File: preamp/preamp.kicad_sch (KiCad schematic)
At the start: 20 parts, among them J1 XLR3_AudioJack2_Combo, J2 Output, J3 Conn_Coaxial, J4 AudioJack3_Switch, U1 SSM2019

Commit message: Prepare for routing
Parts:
- removed unit 2 of J1
- C7: renamed from C?; footprint Capacitor_THT:C_Disc_D3.0mm_W1.6mm_P2.50mm -> Capacitor_THT:C_Rect_L7.0mm_W2.5mm_P5.00mm
- J1: footprint Connector_Audio:Jack_XLR-6.35mm_Neutrik_NCJ9FI-V-0_Vertical -> Connector_Audio:Jack_XLR_Neutrik_NC3FAAH2_Horizontal

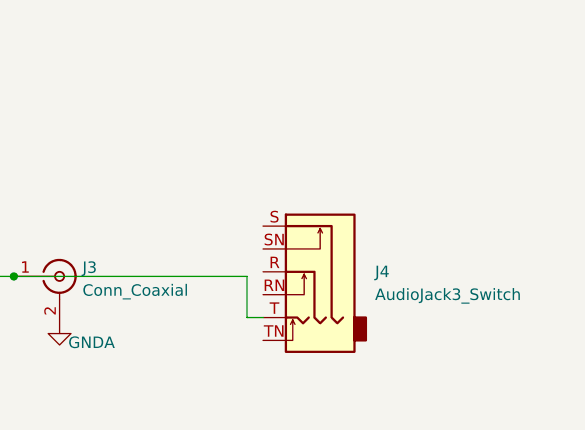
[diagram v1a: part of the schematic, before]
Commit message: Add RCA Plug
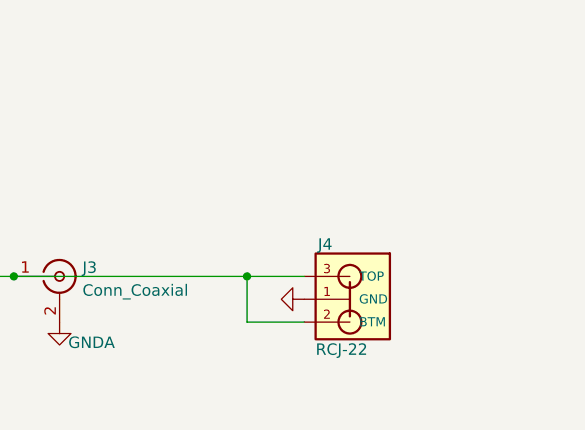
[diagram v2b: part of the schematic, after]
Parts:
- removed J4: AudioJack3_Switch, Connector_Audio:Jack_6.35mm_Neutrik_NMJ6HFD2-AU_Horizontal, symbol Connector:AudioJack3_Switch
- added J4: RCJ-22, rcj-22:rcj-22, symbol rcj-22:RCJ-22
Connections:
- net GNDA: now also J4.1 (GND)
- net at C7.2, J2.2 (Pin_2), J3.1 (In): now also J4.2 (BTM), J4.3 (TOP)
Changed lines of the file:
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@@
   (junction (at 69.85 62.738) (diameter 0) (color 0 0 0 0)
+  )
+  (junction (at 203.708 83.566) (diameter 0) (color 0 0 0 0)
   )
   (junction (at 98.298 82.55) (diameter 0) (color 0 0 0 0)
@@
     (stroke (width 0) (type default) (color 0 0 0 0))
   )
+  (wire (pts (xy 210.058 88.646) (xy 203.708 88.646))
+    (stroke (width 0) (type default) (color 0 0 0 0))
+  )
   (wire (pts (xy 100.076 74.93) (xy 90.678 74.93))
     (stroke (width 0) (type default) (color 0 0 0 0))
   )
-  (wire (pts (xy 203.708 88.138) (xy 205.486 88.138))
-    (stroke (width 0) (type default) (color 0 0 0 0))
-  )
   (wire (pts (xy 109.728 74.93) (xy 114.808 74.93))
     (stroke (width 0) (type default) (color 0 0 0 0))
@@
     (stroke (width 0) (type default) (color 0 0 0 0))
   )
-  (wire (pts (xy 203.708 83.566) (xy 203.708 88.138))
+  (wire (pts (xy 203.708 88.646) (xy 203.708 83.566))
+    (stroke (width 0) (type default) (color 0 0 0 0))
+  )
+  (wire (pts (xy 203.708 83.566) (xy 210.058 83.566))
     (stroke (width 0) (type default) (color 0 0 0 0))
   )
@@
     (pin "1")
     (pin "2")
+  )
+  (symbol (lib_id "rcj-22:RCJ-22") (at 213.868 86.106 0) (mirror y) (unit 1)
+    (in_bom yes) (on_board yes)
+    (property "Reference" "J4" (id 0) (at 211.582 80.01 0)
+      (effects (font (size 1.27 1.27)) (justify right))
+    )
+    (property "Value" "RCJ-22" (id 1) (at 211.328 91.694 0)
+      (effects (font (size 1.27 1.27)) (justify right))
+    )
+    (property "Footprint" "rcj-22:rcj-22" (id 2) (at 215.773 94.996 0)
+      (effects (font (size 1.27 1.27)) (justify bottom) hide)
+    )
+    (property "Datasheet" "" (id 3) (at 198.628 96.266 0)
+      (effects (font (size 1.27 1.27)) hide)
+    )
+    (pin "1")
+    (pin "2")
+    (pin "3")
   )
   (symbol (lib_id "power:GNDA") (at 69.85 62.738 90) (unit 1)
@@
     (pin "2")
   )
-  (symbol (lib_id "Connector:AudioJack3_Switch") (at 210.566 83.058 0) (mirror y) (unit 1)
-    (in_bom yes) (on_board yes) (fields_autoplaced)
-    (property "Reference" "J4" (id 0) (at 217.932 83.0579 0)
-      (effects (font (size 1.27 1.27)) (justify right))
-    )
-    (property "Value" "AudioJack3_Switch" (id 1) (at 217.932 85.5979 0)
-      (effects (font (size 1.27 1.27)) (justify right))
-    )
-    (property "Footprint" "Connector_Audio:Jack_6.35mm_Neutrik_NMJ6HFD2-AU_Horizontal" (id 2) (at 210.566 83.058 0)
-      (effects (font (size 1.27 1.27)) hide)
-    )
-    (property "Datasheet" "~" (id 3) (at 210.566 83.058 0)
-      (effects (font (size 1.27 1.27)) hide)
-    )
-    (pin "R")
-    (pin "RN")
-    (pin "S")
-    (pin "SN")
-    (pin "T")
-    (pin "TN")
+  (symbol (lib_id "power:GNDA") (at 210.058 86.106 270) (unit 1)
+    (in_bom yes) (on_board yes)
+    (property "Reference" "#PWR0114" (id 0) (at 203.708 86.106 0)
+      (effects (font (size 1.27 1.27)) hide)
+    )
+    (property "Value" "GNDA" (id 1) (at 207.01 86.106 90)
+      (effects (font (size 1.27 1.27)) hide)
+    )
+    (property "Footprint" "" (id 2) (at 210.058 86.106 0)
+      (effects (font (size 1.27 1.27)) hide)
+    )
+    (property "Datasheet" "" (id 3) (at 210.058 86.106 0)
+      (effects (font (size 1.27 1.27)) hide)
+    )
+    (pin "1")
   )
   (symbol (lib_id "Device:R") (at 125.73 88.646 0) (unit 1)
@@
       (reference "#PWR0113") (unit 1) (value "GNDA") (footprint "")
     )
+    (path "/50b62985-5c41-43d8-8eca-45c44da7a474"
+      (reference "#PWR0114") (unit 1) (value "GNDA") (footprint "")
+    )
     (path "/733d99b9-c352-4025-9874-def9c4043f46"
       (reference "BT1") (unit 1) (value "Battery_Cell") (footprint "Connector_BarrelJack:BarrelJack_GCT_DCJ200-10-A_Horizontal")
@@
       (reference "J3") (unit 1) (value "Conn_Coaxial") (footprint "")
     )
-    (path "/433c7195-f7a3-46c0-81d5-e2481ad91062"
-      (reference "J4") (unit 1) (value "AudioJack3_Switch") (footprint "Connector_Audio:Jack_6.35mm_Neutrik_NMJ6HFD2-AU_Horizontal")
+    (path "/222e402d-6f3c-4794-9a56-838186e25f8d"
+      (reference "J4") (unit 1) (value "RCJ-22") (footprint "rcj-22:rcj-22")
     )
     (path "/97e15be0-9a57-49c0-be3e-b30325956243"

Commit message: Routing of preamp
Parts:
- removed J2: Output, TerminalBlock_RND:TerminalBlock_RND_205-00045_1x02_P5.00mm_Horizontal, symbol Connector:Screw_Terminal_01x02
- removed J3: Conn_Coaxial, symbol Connector:Conn_Coaxial
- removed J4: RCJ-22, rcj-22:rcj-22, symbol rcj-22:RCJ-22
- added H1, H2: MountingHole, MountingHole:MountingHole_3.2mm_M3_DIN965, symbol Mechanical:MountingHole
- added J2: RCJ-22, rcj-22:rcj-22, symbol rcj-22:RCJ-22
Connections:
- net GNDA: now also J2.1 (GND)
- net at C7.2: now also J2.2 (BTM), J2.3 (TOP)

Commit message: Add mounting holes
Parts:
- added H3, H4: MountingHole, MountingHole:MountingHole_3.2mm_M3_DIN965, symbol Mechanical:MountingHole
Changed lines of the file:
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@@
     (pin "3")
+  )
+  (symbol (lib_id "Mechanical:MountingHole") (at 60.96 114.554 0) (unit 1)
+    (in_bom yes) (on_board yes) (fields_autoplaced)
+    (property "Reference" "H3" (id 0) (at 63.754 113.2839 0)
+      (effects (font (size 1.27 1.27)) (justify left))
+    )
+    (property "Value" "MountingHole" (id 1) (at 63.754 115.8239 0)
+      (effects (font (size 1.27 1.27)) (justify left))
+    )
+    (property "Footprint" "MountingHole:MountingHole_3.2mm_M3_DIN965" (id 2) (at 60.96 114.554 0)
+      (effects (font (size 1.27 1.27)) hide)
+    )
+    (property "Datasheet" "~" (id 3) (at 60.96 114.554 0)
+      (effects (font (size 1.27 1.27)) hide)
+    )
   )
   (symbol (lib_id "Device:C_Small") (at 100.076 77.47 0) (unit 1)
@@
     (pin "T")
   )
+  (symbol (lib_id "Mechanical:MountingHole") (at 61.214 120.142 0) (unit 1)
+    (in_bom yes) (on_board yes) (fields_autoplaced)
+    (property "Reference" "H4" (id 0) (at 64.008 118.8719 0)
+      (effects (font (size 1.27 1.27)) (justify left))
+    )
+    (property "Value" "MountingHole" (id 1) (at 64.008 121.4119 0)
+      (effects (font (size 1.27 1.27)) (justify left))
+    )
+    (property "Footprint" "MountingHole:MountingHole_3.2mm_M3_DIN965" (id 2) (at 61.214 120.142 0)
+      (effects (font (size 1.27 1.27)) hide)
+    )
+    (property "Datasheet" "~" (id 3) (at 61.214 120.142 0)
+      (effects (font (size 1.27 1.27)) hide)
+    )
+  )
   (symbol (lib_id "power:GNDA") (at 98.298 87.63 0) (unit 1)
     (in_bom yes) (on_board yes) (fields_autoplaced)
@@
       (reference "H2") (unit 1) (value "MountingHole") (footprint "MountingHole:MountingHole_3.2mm_M3_DIN965")
     )
+    (path "/69e4ce63-3424-4243-9653-935f6005fe6b"
+      (reference "H3") (unit 1) (value "MountingHole") (footprint "MountingHole:MountingHole_3.2mm_M3_DIN965")
+    )
+    (path "/dd836eca-f0db-4277-ac14-8f848179e84a"
+      (reference "H4") (unit 1) (value "MountingHole") (footprint "MountingHole:MountingHole_3.2mm_M3_DIN965")
+    )
     (path "/dd05fd78-4b95-4f67-9ddc-b8c882850ad2"

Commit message: Prepare for milling
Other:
- company: (none) -> Besmer Labs
- title: (none) -> XLR Preamp
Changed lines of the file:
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@@
 (kicad_sch (version 20211123) (generator eeschema)
   (paper "A4")
+  (title_block
+    (title "XLR Preamp")
+    (date "2023-05-01")
+    (rev "1.0")
+    (company "Besmer Labs")
+  )
   (junction (at 109.728 74.93) (diameter 0) (color 0 0 0 0)
   )

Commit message: Update board with the findings of the pcb
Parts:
- R3, R4: value 2k2 -> 10k
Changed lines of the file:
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@@
   (title_block
     (title "XLR Preamp")
-    (date "2023-05-01")
-    (rev "1.0")
+    (date "2023-05-03")
+    (rev "1.1")
     (company "Besmer Labs")
   )
@@
       (effects (font (size 1.27 1.27)) (justify left))
     )
-    (property "Value" "2k2" (id 1) (at 127.254 90.17 0)
+    (property "Value" "10k" (id 1) (at 127.254 90.17 0)
       (effects (font (size 1.27 1.27)) (justify left))
     )
@@
       (effects (font (size 1.27 1.27)) (justify left))
     )
-    (property "Value" "2k2" (id 1) (at 127.254 80.264 0)
+    (property "Value" "10k" (id 1) (at 127.254 80.264 0)
       (effects (font (size 1.27 1.27)) (justify left))
     )
@@
     )
     (path "/d9e1c057-b9b0-4660-8426-ad97b16c6bbc"
-      (reference "R3") (unit 1) (value "2k2") (footprint "Resistor_THT:R_Axial_DIN0207_L6.3mm_D2.5mm_P7.62mm_Horizontal")
+      (reference "R3") (unit 1) (value "10k") (footprint "Resistor_THT:R_Axial_DIN0207_L6.3mm_D2.5mm_P7.62mm_Horizontal")
     )
     (path "/56f0c233-453e-449d-9554-cc38d9f909d8"
-      (reference "R4") (unit 1) (value "2k2") (footprint "Resistor_THT:R_Axial_DIN0207_L6.3mm_D2.5mm_P7.62mm_Horizontal")
+      (reference "R4") (unit 1) (value "10k") (footprint "Resistor_THT:R_Axial_DIN0207_L6.3mm_D2.5mm_P7.62mm_Horizontal")
     )
     (path "/c063a6c4-b4c8-4a64-88fd-f1066955e6e9"

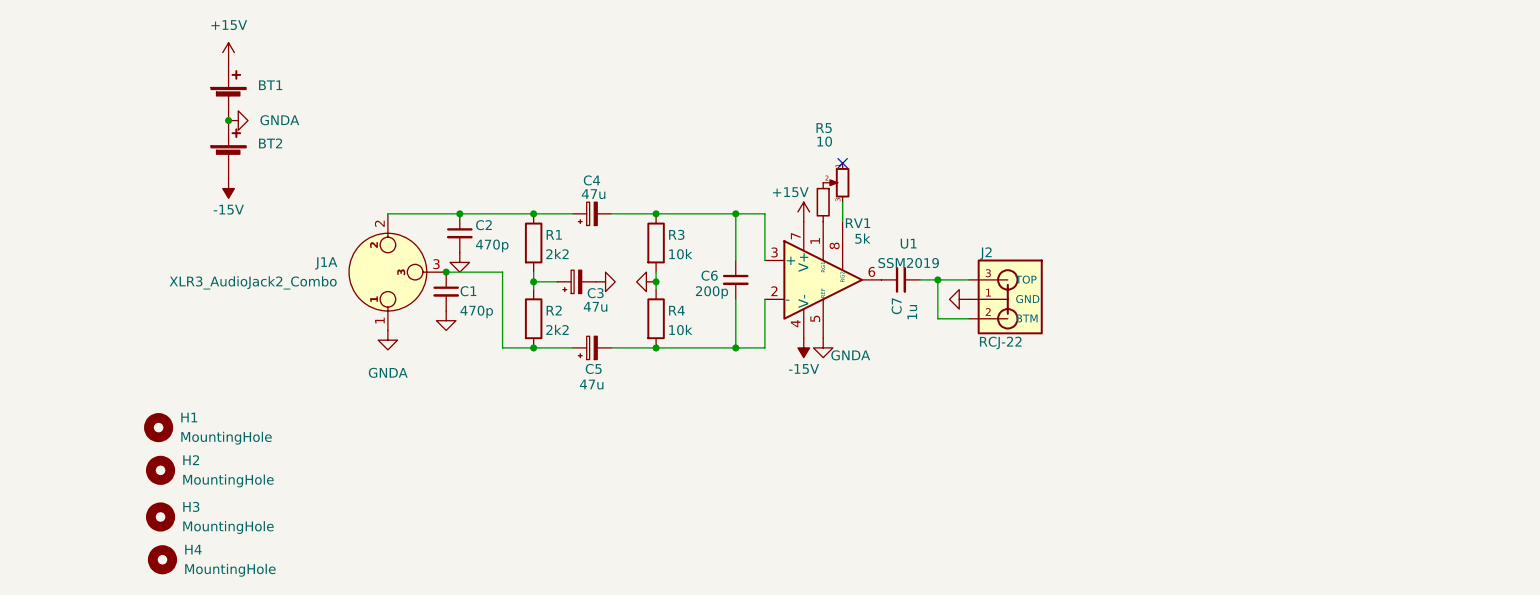
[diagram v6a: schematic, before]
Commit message: Replace the RCA jack with an Audio Jack
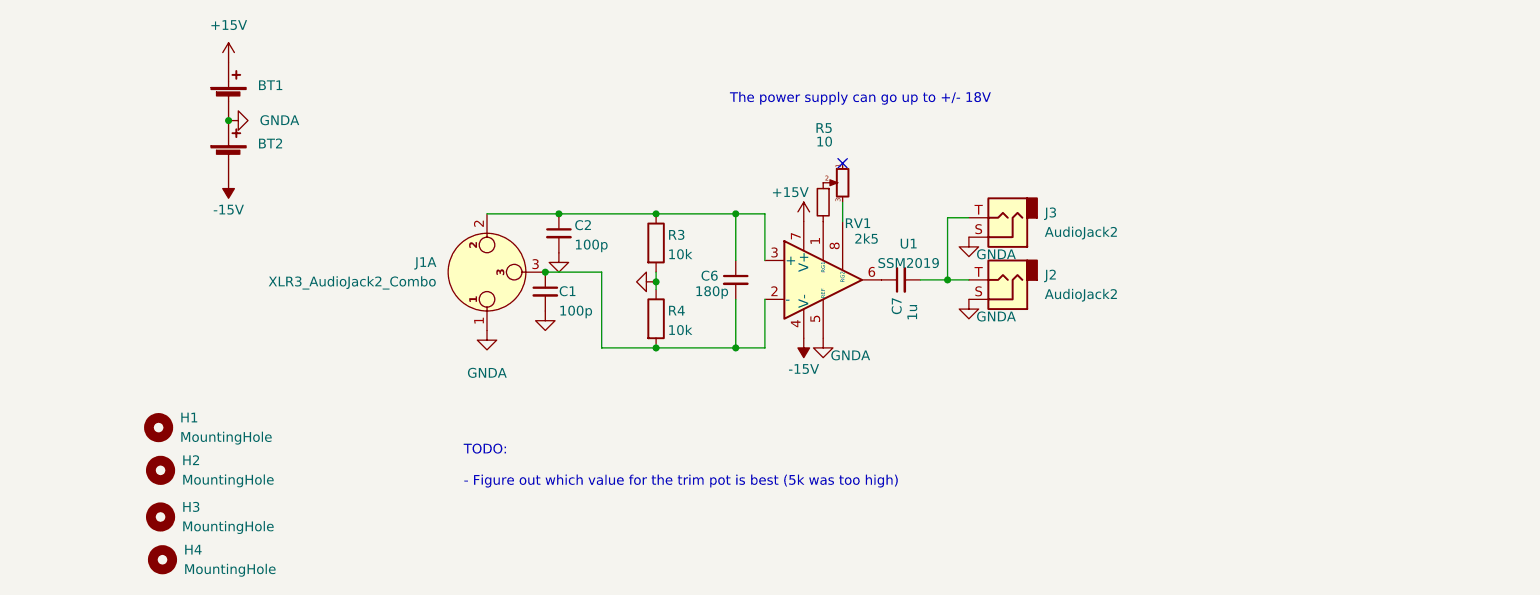
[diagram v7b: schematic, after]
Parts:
- removed C3, C4, C5: 47u, Capacitor_THT:CP_Radial_D6.3mm_P2.50mm, symbol Device:C_Polarized_Small
- removed J2: RCJ-22, rcj-22:rcj-22, symbol rcj-22:RCJ-22
- removed R1, R2: 2k2, Resistor_THT:R_Axial_DIN0207_L6.3mm_D2.5mm_P7.62mm_Horizontal, symbol Device:R
- added J2: AudioJack2, Connector_Audio:Jack_6.35mm_Neutrik_NMJ6HFD2_Horizontal, symbol Connector:AudioJack2
- added J3: AudioJack2, Connector_Audio:Jack_3.5mm_CUI_SJ-3523-SMT_Horizontal, symbol Connector:AudioJack2
- C1, C2: value 470p -> 100p
- C6: value 200p -> 180p
- RV1: value 5k -> 2k5
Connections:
- net GNDA: now also J2.S, J3.S
- net at C1.1, J1.3: now also C6.2, R4.2, U1.2 (-)
- net at C7.2: now also J2.T, J3.T
- net at C2.1, J1.2: now also C6.1, R3.1, U1.3 (+)
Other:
- note added: "TODO: - Figure out which value for the trim pot is best (5k was too high)"
- note added: "The power supply can go up to +/- 18V"
- moved on the sheet: C1, C2, J1A
